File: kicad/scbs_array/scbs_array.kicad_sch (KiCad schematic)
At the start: 33 parts, among them J1 Barrel_Jack, J2 Phoenix MSTBA 1x05 5.08mm, J3 Conn_01x03_Male, Q1 FQP27P06, U1 WRB1205S-3WR2, U2 WRB1205S-3WR2, U3 WRB1205S-3WR2, U4 WRB1205S-3WR2

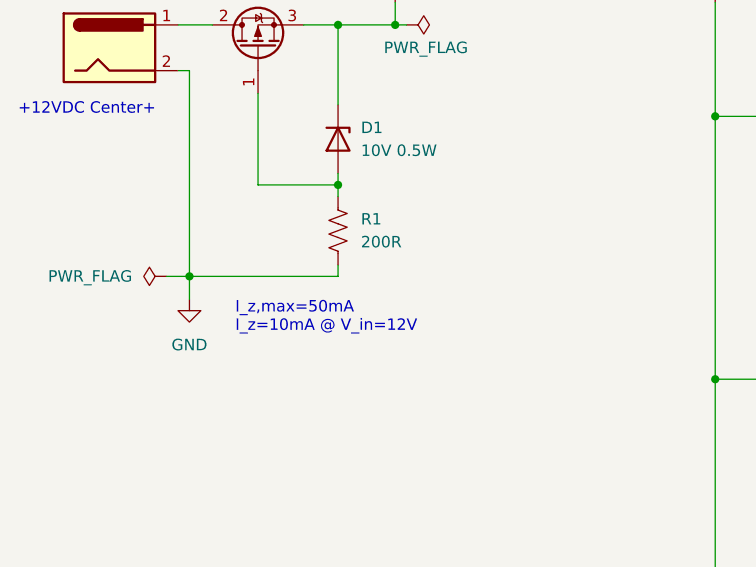
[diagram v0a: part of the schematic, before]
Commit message: Make enclosure CAD
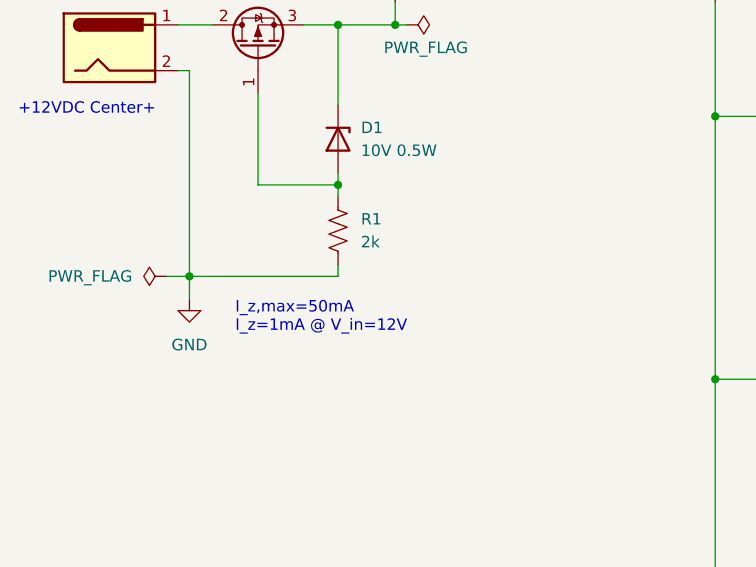
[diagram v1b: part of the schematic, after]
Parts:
- R1: value 200R -> 2k
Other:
- note added: "I_z,max=50mA I_z=1mA @ V_in=12V"
- note removed: "I_z,max=50mA I_z=10mA @ V_in=12V"
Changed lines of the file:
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@@
     (effects (font (size 1.27 1.27)) (justify left bottom))
   )
-  (text "I_z,max=50mA\nI_z=10mA @ V_in=12V" (at 38.1 72.39 0)
+  (text "I_z,max=50mA\nI_z=1mA @ V_in=12V" (at 38.1 72.39 0)
     (effects (font (size 1.27 1.27)) (justify left bottom))
   )
@@
       (effects (font (size 1.27 1.27)) (justify left))
     )
-    (property "Value" "200R" (id 1) (at 52.07 62.2299 0)
+    (property "Value" "2k" (id 1) (at 52.07 62.2299 0)
       (effects (font (size 1.27 1.27)) (justify left))
     )
@@
     )
     (path "/aba6e3da-b649-418e-ab20-797560fadc22"
-      (reference "R1") (unit 1) (value "200R") (footprint "Resistor_SMD:R_0805_2012Metric")
+      (reference "R1") (unit 1) (value "2k") (footprint "Resistor_SMD:R_0805_2012Metric")
     )
     (path "/0f960744-e721-48cb-af3d-c1f0f2d83444"

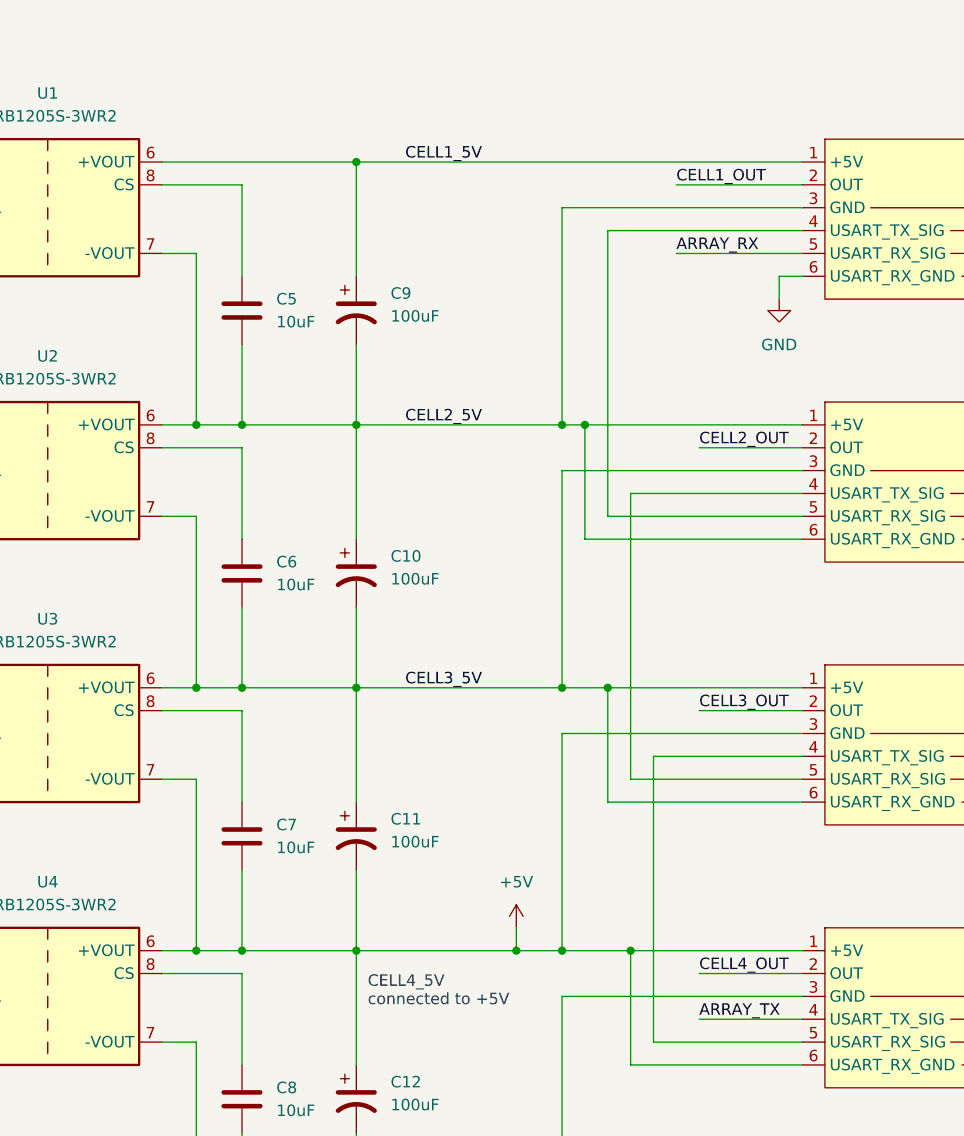
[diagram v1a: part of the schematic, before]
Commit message: Add CELLSIM 4S documentation
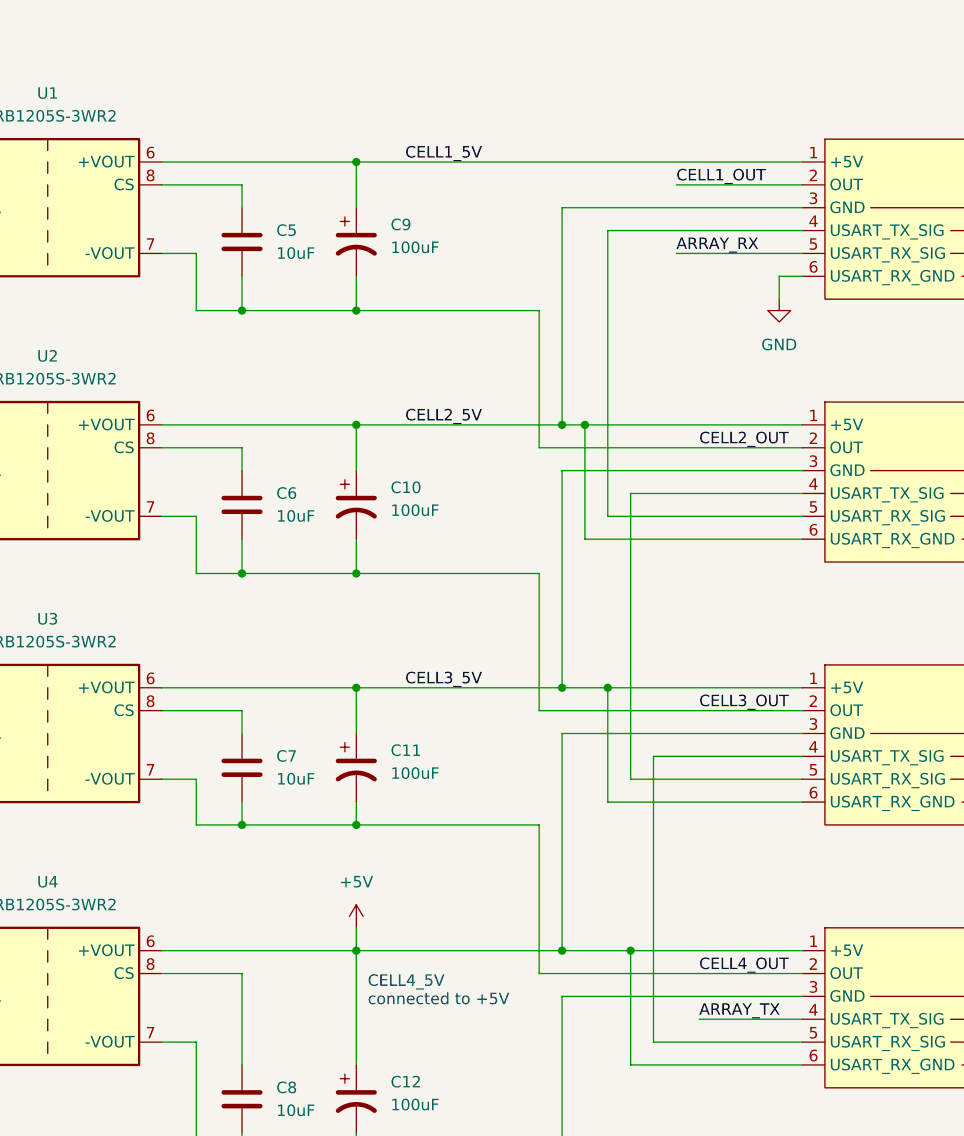
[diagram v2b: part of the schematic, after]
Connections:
- net +5V: no longer C11.2, C7.2, U3.7 (-VOUT)
- net CELL2_5V: no longer C5.2, C9.2, U1.7 (-VOUT)
- net CELL2_OUT: now also C5.2, C9.2, U1.7 (-VOUT)
- net CELL3_5V: no longer C10.2, C6.2, U2.7 (-VOUT)
- net CELL3_OUT: now also C10.2, C6.2, U2.7 (-VOUT)
- net CELL4_OUT: now also C11.2, C7.2, U3.7 (-VOUT)
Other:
- moved on the sheet: C10, C11, C5, C6, C7, C9
